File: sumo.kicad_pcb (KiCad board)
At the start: 2 copper layers, 76.2 x 81.3 mm, 51 parts, among them Q1 BPW40, Q2 BPW40, SW1 SW_Push, SW2 SW_DIP_x01, T1 Screw_Terminal_01x04, T2 Screw_Terminal_01x04, T3 Screw_Terminal_01x04, T4 Screw_Terminal_01x04, T5 Screw_Terminal_01x04, U1 PIC16F628A-IP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

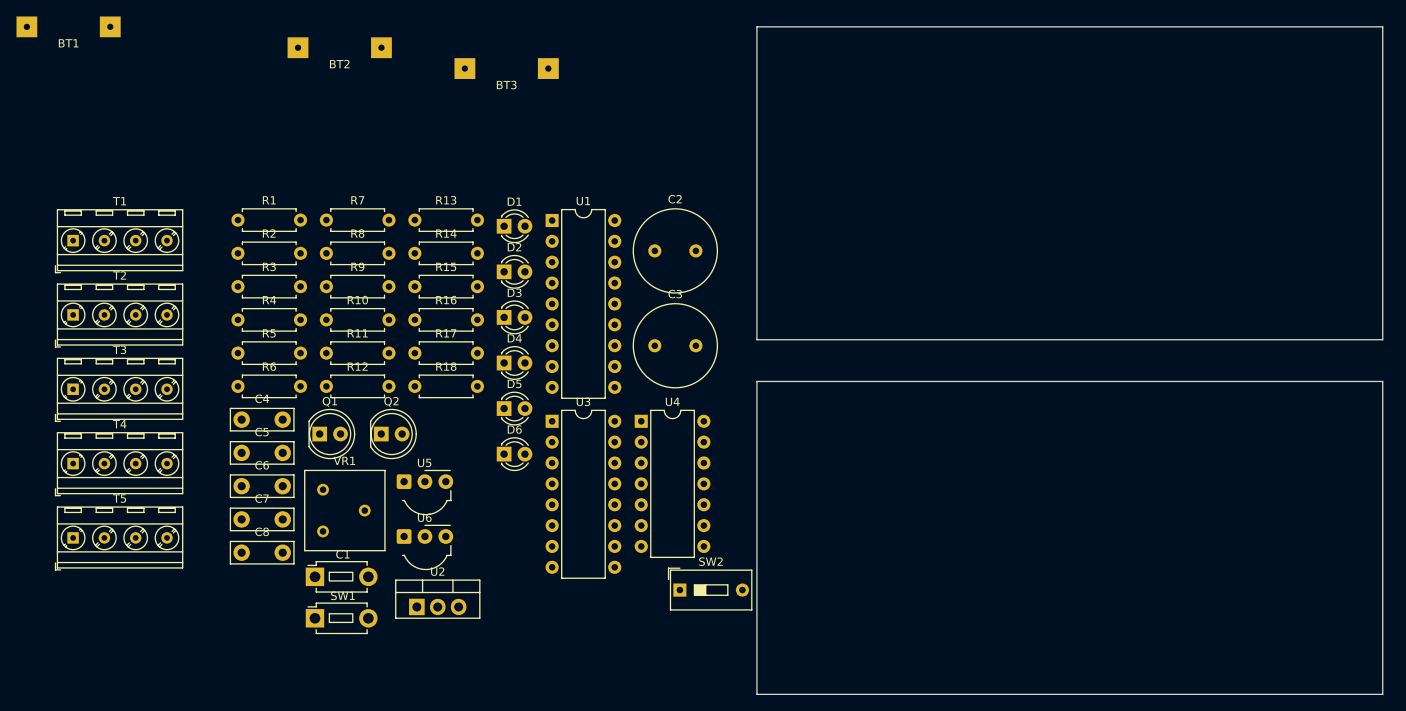
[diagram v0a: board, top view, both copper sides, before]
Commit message: fix battery footprint
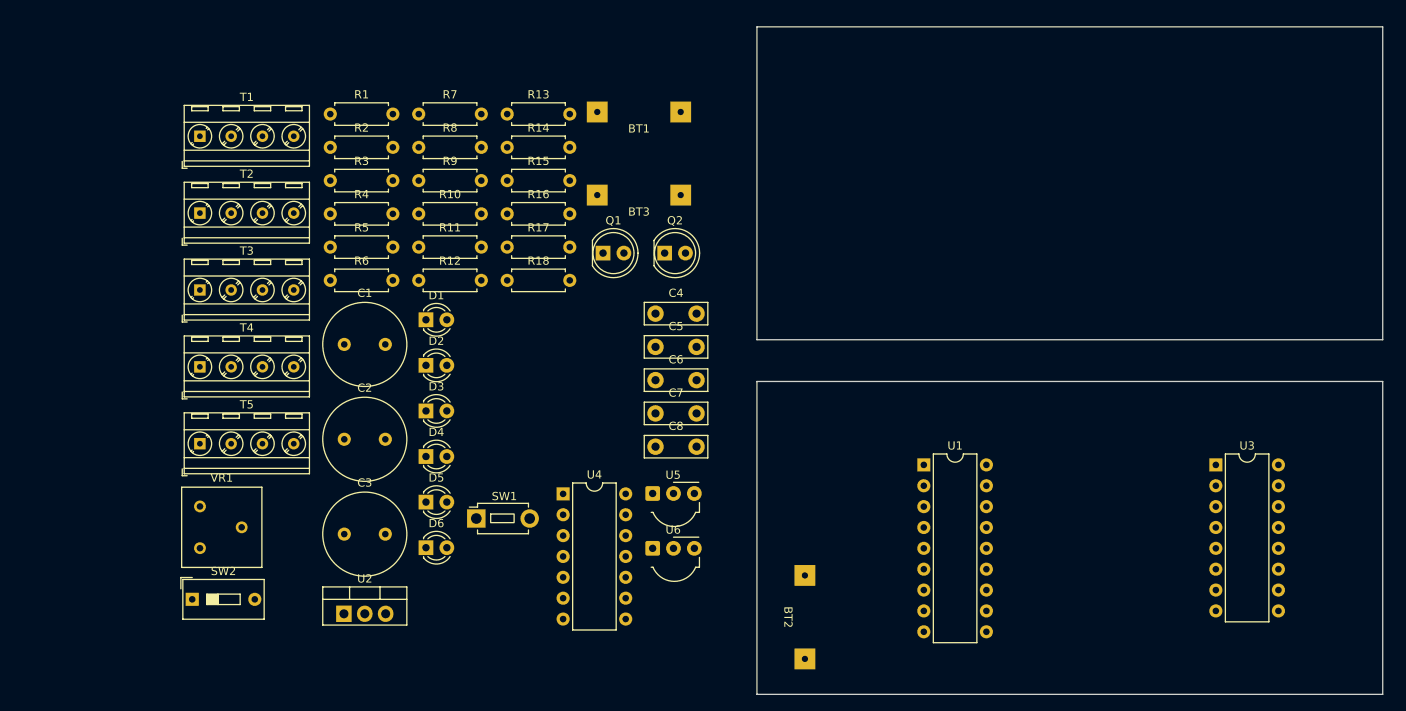
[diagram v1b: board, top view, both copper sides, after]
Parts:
- C1: footprint Button_Switch_THT:SW_PUSH_1P1T_6x3.5mm_H5.0_APEM_MJTP1250 -> Capacitor_THT:C_Radial_D10.0mm_H12.5mm_P5.00mm
- moved BT2 86.0 mm to (130.3, 122.7), turned to -90 degrees
- moved U3 81.0 mm to (182.9, 104.1)
- moved BT1 70.2 mm to (112.6, 63.7)
- moved SW2 59.4 mm to (58.2, 120.5)
- moved U1 54.2 mm to (147.3, 104.1)
- moved C4 52.0 mm to (114.7, 85.7)
- moved C5 52.0 mm to (114.7, 89.8)
- moved C6 52.0 mm to (114.7, 93.8)
- moved C7 52.0 mm to (114.7, 97.9)
- moved C8 52.0 mm to (114.7, 101.9)
- moved C2 44.2 mm to (76.8, 101.0)
- moved C3 44.2 mm to (76.8, 112.6)
- moved Q1 40.9 mm to (108.3, 78.3)
- moved Q2 40.9 mm to (115.8, 78.3)
- moved U5 30.3 mm to (114.3, 107.6)
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
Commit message: motor driver
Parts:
- moved T4 138.2 mm to (195.6, 114.3), turned to -90 degrees
- moved R3 127.8 mm to (199.4, 99.1), turned to -90 degrees
- moved T3 120.0 mm to (175.3, 113.0), turned to -90 degrees
- moved SW2 118.2 mm to (174.0, 96.5)
- moved R2 117.8 mm to (185.4, 106.7), turned to 90 degrees
- moved T1 98.0 mm to (140.9, 118.1), turned to -90 degrees
- moved C2 97.3 mm to (174.0, 102.9), turned to -90 degrees
- moved T2 93.0 mm to (148.6, 99.1)
- moved R1 79.4 mm to (143.5, 101.6), turned to -90 degrees
- moved C1 59.7 mm to (135.9, 97.9), turned to -90 degrees
- moved BT3 58.2 mm to (163.8, 101.6), turned to -90 degrees
- moved U2 57.0 mm to (133.0, 113.4), turned to 90 degrees
- moved SW1 45.5 mm to (138.3, 113.0)
- moved U3 6.47 mm to (181.6, 110.5)
- moved U1 1.80 mm to (148.6, 105.4)
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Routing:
- net GNDREF: track 0.00 -> 126.6 mm
- net Net-(U3-VCC1): track 0.00 -> 88.9 mm
- net +5V: track 0.00 -> 70.9 mm
- net Net-(U3-EN3,4): track 0.00 -> 31.7 mm
- net Net-(BT3-+): track 0.00 -> 14.0 mm
- net Net-(T2-Pin_1): track 0.00 -> 14.0 mm
- net Net-(T2-Pin_4): track 0.00 -> 12.7 mm
- net Net-(T2-Pin_2): track 0.00 -> 10.2 mm
- net Net-(T1-Pin_4): track 0.00 -> 9.25 mm
- net Net-(T1-Pin_3): track 0.00 -> 8.73 mm
- net Net-(T1-Pin_2): track 0.00 -> 8.20 mm
- net Net-(U1-~{MCLR}/Vpp/RA5): track 0.00 -> 8.16 mm
- net Net-(BT3--): track 0.00 -> 8.13 mm
- net Net-(T1-Pin_1): track 0.00 -> 7.67 mm
- net Net-(U3-EN1,2): track 0.00 -> 7.61 mm
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
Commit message: schematic updates
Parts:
- added D7: IR LED, LED_THT:LED_D5.0mm_IRBlack, F.Cu at (105.4, 91.0)
- added D8: IR LED, LED_THT:LED_D5.0mm_IRBlack, F.Cu at (105.4, 96.5)
- added SW3: SW_DIP_x01, Button_Switch_THT:SW_DIP_SPSTx01_Slide_9.78x4.72mm_W7.62mm_P2.54mm, F.Cu at (167.6, 110.5)
- added SW4: SW_DIP_x01, Button_Switch_THT:SW_DIP_SPSTx01_Slide_9.78x4.72mm_W7.62mm_P2.54mm, F.Cu at (168.9, 118.1)
- D1, D2, D5, D6: footprint LED_THT:LED_D3.0mm -> LED_THT:LED_D5.0mm
- D3, D4: footprint LED_THT:LED_D3.0mm_IRBlack -> LED_THT:LED_D5.0mm_IRBlack
- moved T5 114.1 mm to (172.1, 85.0), turned to 180 degrees
- moved R4 104.1 mm to (179.1, 68.6), turned to 90 degrees
- moved U5 100.0 mm to (200.7, 57.2), turned to 180 degrees
- moved D1 97.7 mm to (179.1, 54.6), turned to -90 degrees
- moved R5 96.8 mm to (171.4, 68.6), turned to 90 degrees
- moved U4 95.6 mm to (191.8, 71.1)
- moved R6 93.3 mm to (168.3, 78.7), turned to 90 degrees
- moved R12 90.1 mm to (175.3, 71.1), turned to -90 degrees
- moved D5 86.1 mm to (153.7, 54.6), turned to -90 degrees
- moved D6 81.4 mm to (144.8, 57.1), turned to -90 degrees
- moved C3 70.4 mm to (138.5, 78.8), turned to -90 degrees
- moved R15 68.5 mm to (164.5, 78.7), turned to 90 degrees
- moved Q1 66.7 mm to (171.5, 57.2), turned to 90 degrees
- moved R14 64.8 mm to (161.3, 68.6), turned to 90 degrees
- moved U6 61.6 mm to (137.2, 57.1), turned to 180 degrees
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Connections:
- C3 pad 1: unconnected-(C3-Pad1) -> +6V
- C3 pad 2: unconnected-(C3-Pad2) -> GNDREF
- R12 pad 2: Net-(T5-Pin_3) -> Net-(T5-Pin_1)
- R15 pad 1: Net-(T5-Pin_2) -> Net-(T5-Pin_3)
- R6 pad 1: Net-(T5-Pin_1) -> Net-(T5-Pin_2)
- U1 pad 15: unconnected-(U1-CLKOUT/OSC2/RA6-Pad15) -> Net-(U1-CLKOUT/OSC2/RA6)
- U1 pad 16: unconnected-(U1-CLKIN/OSC1/RA7-Pad16) -> Net-(U1-CLKIN/OSC1/RA7)
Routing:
- net GNDREF: track 126.6 -> 246.3 mm
- net +6V: track 0.00 -> 93.9 mm
- net Net-(D6-K): track 0.00 -> 38.2 mm
- net +5V: track 70.9 -> 93.5 mm
- net Net-(Q1-C): track 0.00 -> 15.3 mm
- net Net-(Q2-C): track 0.00 -> 15.2 mm
- net Net-(U6-Vs): track 0.00 -> 11.9 mm
- net Net-(T5-Pin_1): track 0.00 -> 7.67 mm
- net Net-(T5-Pin_4): track 0.00 -> 7.62 mm
- net Net-(U1-CLKOUT/OSC2/RA6): track 0.00 -> 7.18 mm
- net Net-(T5-Pin_3): track 0.00 -> 6.35 mm
- net Net-(T5-Pin_2): track 0.00 -> 6.31 mm
- net Net-(D6-A): track 0.00 -> 3.82 mm
- net Net-(D1-A): track 0.00 -> 3.82 mm
- net Net-(D5-A): track 0.00 -> 3.81 mm
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
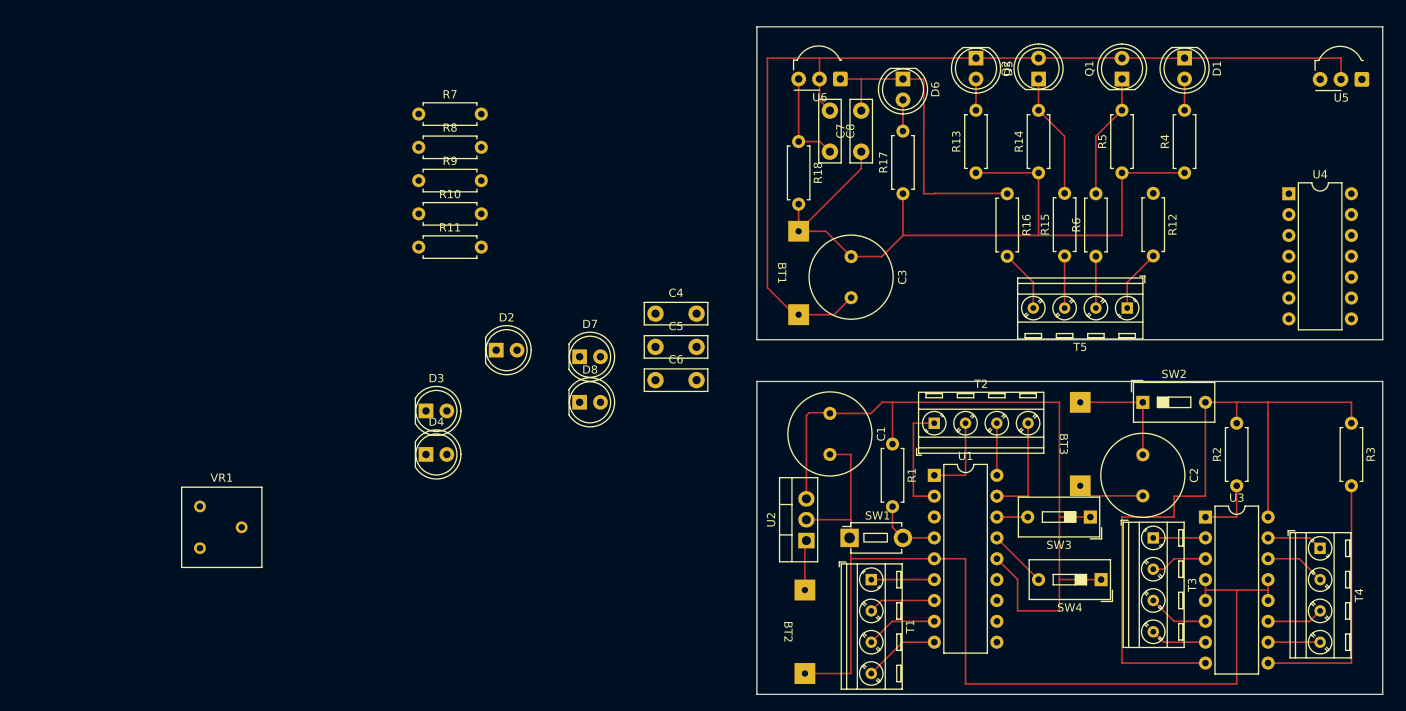
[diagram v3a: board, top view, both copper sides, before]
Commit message: connect grounds
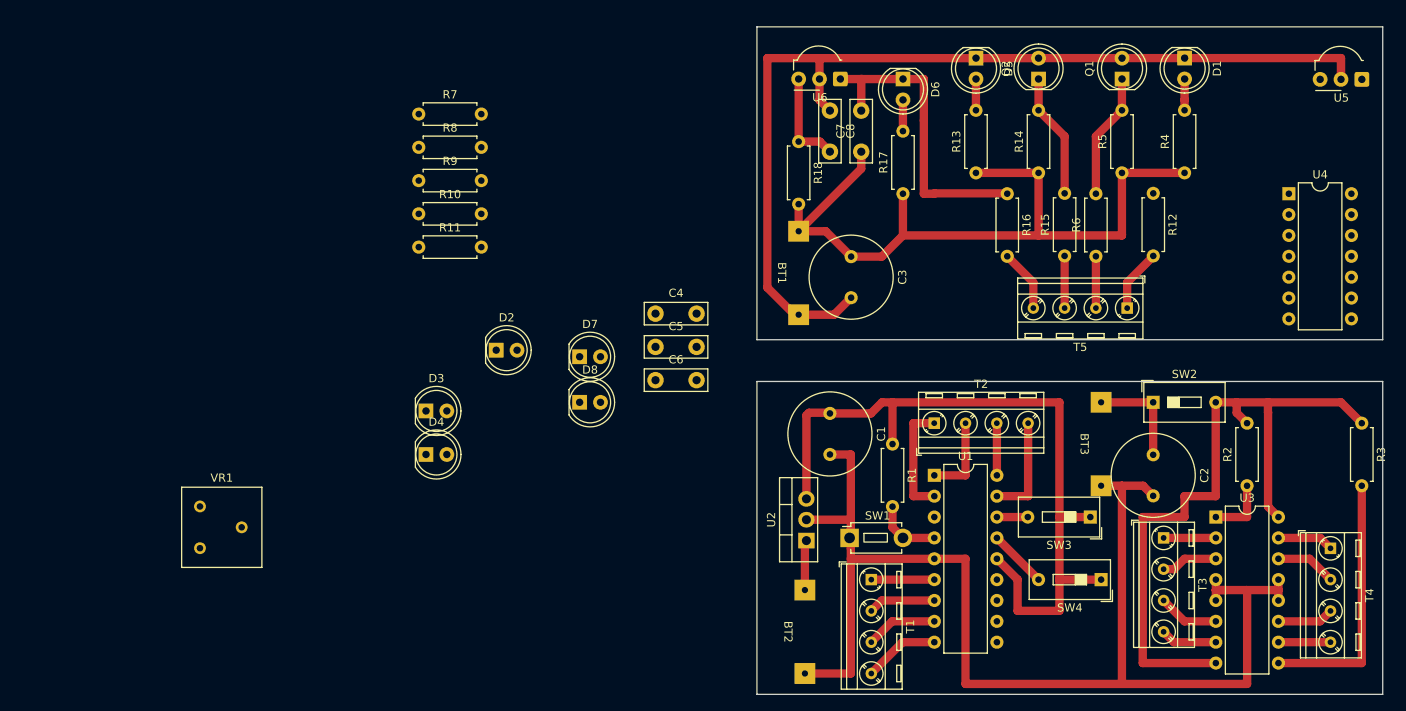
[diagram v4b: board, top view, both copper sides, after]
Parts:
- moved BT3 2.54 mm to (166.4, 101.6)
- moved R2 1.26 mm to (186.7, 106.7)
- moved R3 1.26 mm to (200.7, 99.1)
- moved T3 1.26 mm to (176.5, 113.0)
- moved C2 1.26 mm to (175.2, 102.9)
- moved SW2 1.26 mm to (175.2, 96.5)
- moved T4 1.26 mm to (196.8, 114.3)
- moved U3 1.26 mm to (182.9, 110.5)
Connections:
- BT3 pad 2: Net-(BT3--) -> GNDREF
- C2 pad 2: Net-(BT3--) -> GNDREF
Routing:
- net GNDREF: track 246.3 -> 279.8 mm
- net Net-(BT3--): track 8.13 -> 0.00 mm
- net Net-(U3-VCC1): track 88.9 -> 85.9 mm
- net Net-(BT3-+): track 14.0 -> 12.7 mm

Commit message: sensors
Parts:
- T2, T5: footprint TerminalBlock_MetzConnect:TerminalBlock_MetzConnect_Type086_RT03404HBLC_1x04_P3.81mm_Horizontal -> TerminalBlock_MetzConnect:TerminalBlock_MetzConnect_Type086_RT03405HBLC_1x05_P3.81mm_Horizontal
- moved R10 115.3 mm to (200.7, 63.5), turned to -90 degrees
- moved R11 99.8 mm to (185.4, 71.1), turned to 90 degrees
- moved D2 96.0 mm to (185.4, 57.1), turned to -90 degrees
- moved C5 86.3 mm to (196.8, 63.6), turned to -90 degrees
- moved C6 83.4 mm to (191.8, 62.2), turned to 90 degrees
- moved U4 11.7 mm to (199.4, 80.0), turned to -90 degrees
- moved U5 5.08 mm to (195.6, 57.1), turned to 0 degrees
- moved R1 5.08 mm to (143.5, 96.5)
- moved SW3 1.31 mm to (168.9, 110.5)
- moved D5 1.27 mm to (152.4, 54.6)
- moved Q1 1.27 mm to (170.2, 57.2)
- moved R15 1.27 mm to (163.2, 78.7)
- moved R6 1.27 mm to (167.0, 78.7)
- moved T5 1.27 mm to (170.8, 85.0)
- moved D1 1.27 mm to (177.8, 54.6)
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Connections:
- T2 pad 1: Net-(T2-Pin_1) -> GNDREF
- U1 pad 1: Net-(T2-Pin_2) -> Net-(T2-Pin_3)
- U1 pad 17: Net-(T2-Pin_4) -> Net-(T2-Pin_5)
- U1 pad 18: Net-(T2-Pin_3) -> Net-(T2-Pin_4)
- U1 pad 2: Net-(T2-Pin_1) -> Net-(T2-Pin_2)
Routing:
- net +6V: track 93.9 -> 137.7 mm
- net GNDREF: track 279.8 -> 316.1 mm
- net Net-(D2-K): track 0.00 -> 35.6 mm
- net Net-(T2-Pin_5): track 0.00 -> 16.5 mm
- net Net-(T2-Pin_1): track 14.0 -> 0.00 mm
- net Net-(U5-Vs): track 0.00 -> 13.0 mm
- net Net-(T2-Pin_3): track 6.35 -> 14.0 mm
- net Net-(U1-~{MCLR}/Vpp/RA5): track 8.16 -> 13.2 mm
- net Net-(T2-Pin_2): track 10.2 -> 14.7 mm
- net Net-(D2-A): track 0.00 -> 3.81 mm
- net +5V: track 93.5 -> 89.7 mm
- net Net-(T2-Pin_4): track 12.7 -> 10.2 mm
- net Net-(D6-K): track 38.2 -> 36.9 mm
